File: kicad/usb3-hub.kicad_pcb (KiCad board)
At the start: 6 copper layers, 70 x 140 mm, 218 parts, among them J1001 USB3_A, J101 DISPLAY, J102 USB3_B_Micro, J103 Barrel_Jack_Switch, J201 Conn_01x05_Pin, J301 Debug, J302 Conn_01x03_Pin, J501 USB3_A, J601 USB3_A, J701 USB3_A, J801 USB3_A, J901 USB3_A, Q303 2N7002, SW1001 SW_Push, SW301 SW_Push, SW501 SW_Push, SW601 SW_Push, SW701 SW_Push, SW801 SW_Push, SW901 SW_Push, U1001 AP22804AW5, U201 USB5807, U301 W25Q16JVSS, U302 RP2040, U303 AP22804AW5, U401 TLV1117-33, U402 AP7363C-12E, U501 INA381A1, U502 AP22804AW5, U601 INA381A1, U602 AP22804AW5, U701 INA381A1, U702 AP22804AW5, U801 AP22804AW5, U901 AP22804AW5, Y201 25Mhz, Y301 12Mhz

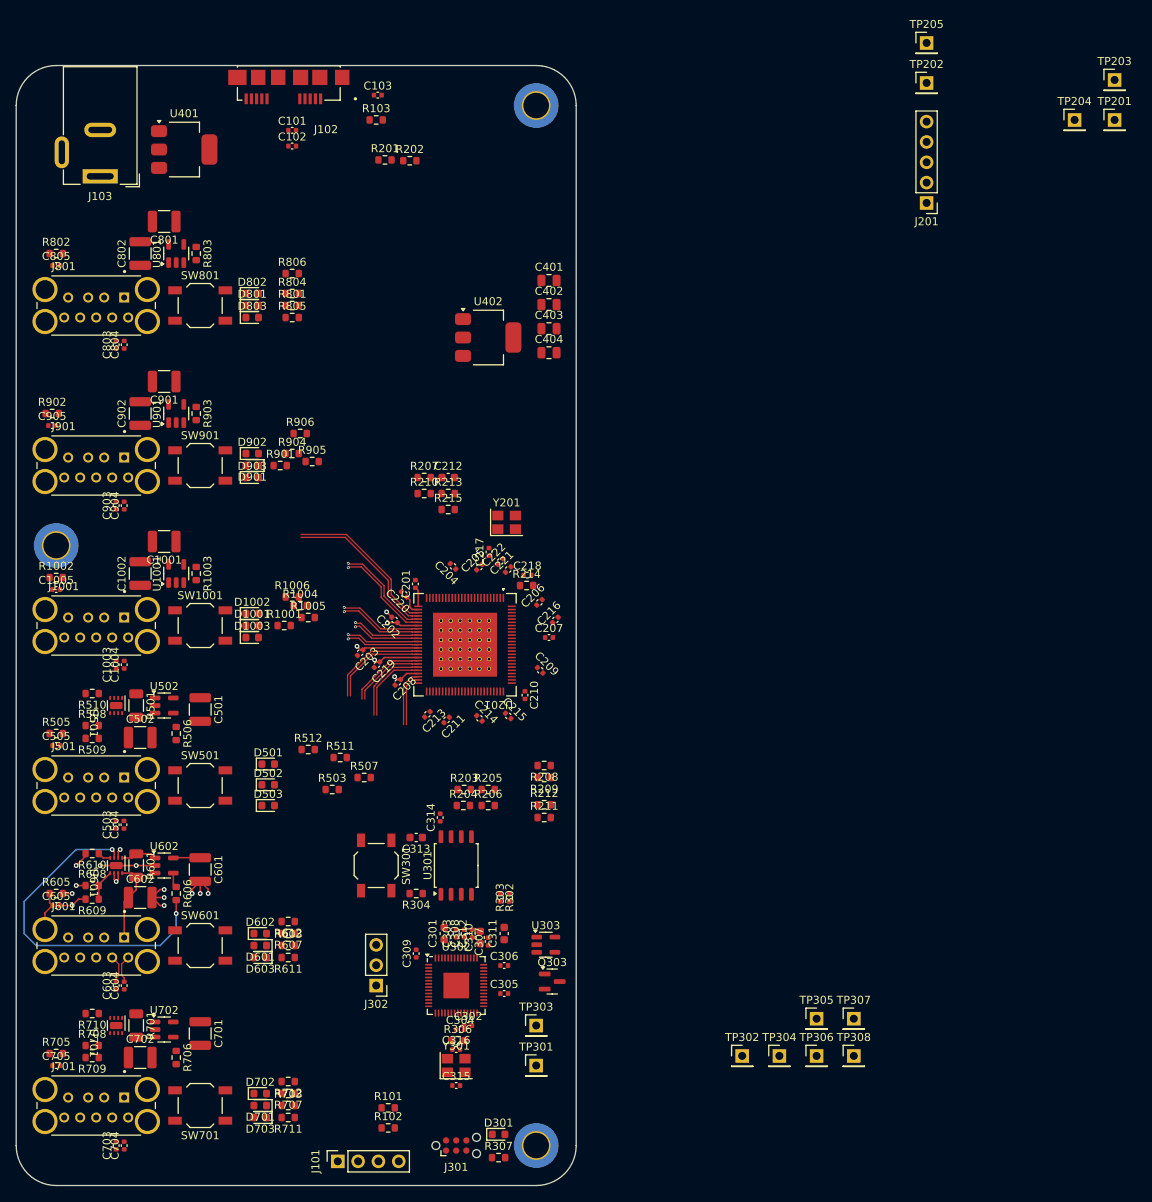
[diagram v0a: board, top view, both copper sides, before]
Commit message: Added first fanout for usb5807
Needs a lot more work, but it is a start, that allows me to concentrate
on the routing of USB signals and have the capacitors relatively close
to the hub controller.
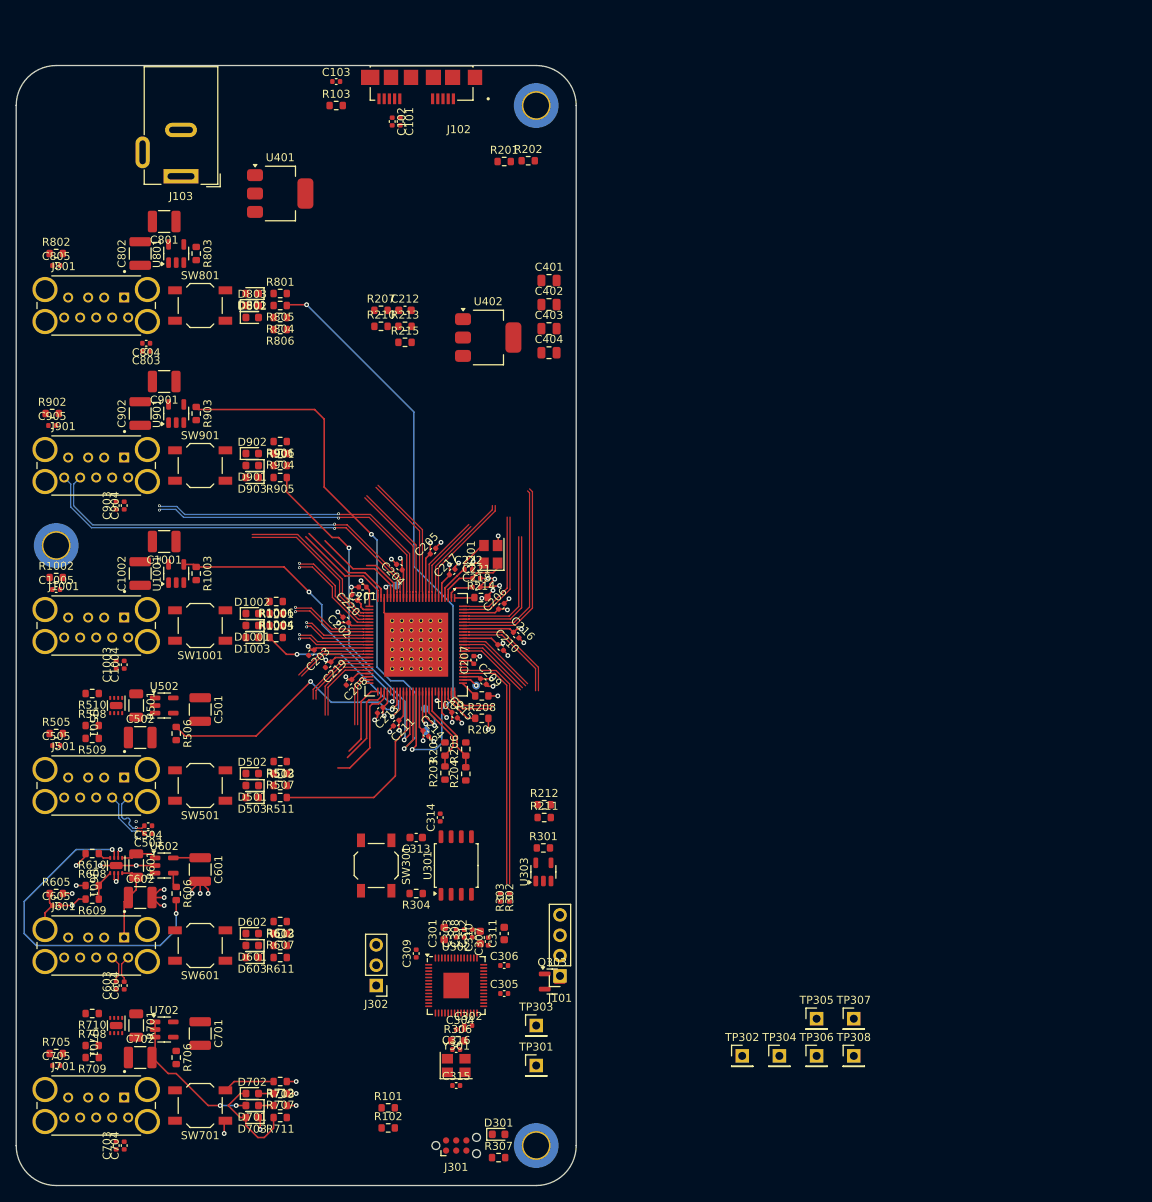
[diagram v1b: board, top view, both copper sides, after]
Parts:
- removed J201: Conn_01x05_Pin, Connector_PinHeader_2.54mm:PinHeader_1x05_P2.54mm_Vertical
- removed TP203: TestPoint, Connector_PinHeader_2.54mm:PinHeader_1x01_P2.54mm_Vertical
- added R301: 100k, Resistor_SMD:R_0603_1608Metric, F.Cu at (165.9, 132.8)
- TP201, TP202, TP204, TP205: footprint Connector_PinHeader_2.54mm:PinHeader_1x01_P2.54mm_Vertical -> TestPoint:TestPoint_Pad_D1.0mm; moved to B.Cu
- moved TP201 115.1 mm to (151.2, 118.2), turned to 180 degrees
- moved TP204 102.9 mm to (147.5, 100.0), turned to 180 degrees
- moved TP202 100.3 mm to (151.1, 115.4), turned to 180 degrees
- moved TP205 98.1 mm to (157.5, 112.5), turned to 180 degrees
- moved J101 36.2 mm to (168.0, 148.8), turned to 180 degrees
- moved C212 21.6 mm to (148.6, 65.6)
- moved R207 21.6 mm to (145.6, 65.6)
- moved R210 21.6 mm to (145.6, 67.6)
- moved R213 21.6 mm to (148.6, 67.6)
- moved R215 21.6 mm to (148.6, 69.6)
- moved J102 16.6 mm to (150.0, 39.2)
- moved R201 14.9 mm to (161.0, 47.0)
- moved R202 14.8 mm to (164.0, 46.9)
- moved C101 13.5 mm to (148.0, 42.0), turned to -90 degrees
- moved U401 13.2 mm to (133.0, 51.0)
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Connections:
- net /Port1/VBUS_HIGH renamed /Port4/VBUS_HIGH
- net /Port1/~{Alert} renamed /Port4/~{Alert}
- net /Port2/VBUS_HIGH renamed /Port5/VBUS_HIGH
- net /Port2/~{Alert} renamed /Port5/~{Alert}
- net /Port3/VBUS_HIGH renamed /Port6/VBUS_HIGH
- net /Port3/~{Alert} renamed /Port6/~{Alert}
- net /Port4/~{Flag} renamed /Port1/~{Flag}
- net /Port5/~{Flag} renamed /Port2/~{Flag}
- net /Port6/~{Flag} renamed /Port3/~{Flag}
- C1002 pad 1: /Port6/VBUS -> /Port3/VBUS
- C1003 pad 2: /Port6/B_SSTX- -> /Port3/B_SSTX-
- C1004 pad 2: /Port6/B_SSTX+ -> /Port3/B_SSTX+
- C1005 pad 1: /Port6/Shield -> /Port3/Shield
- C502 pad 1: /Port1/VBUS -> /Port4/VBUS
- C503 pad 2: /Port1/B_SSTX- -> /Port4/B_SSTX-
- C504 pad 2: /Port1/B_SSTX+ -> /Port4/B_SSTX+
- C505 pad 1: /Port1/Shield -> /Port4/Shield
- C602 pad 1: /Port2/VBUS -> /Port5/VBUS
- C603 pad 2: /Port2/B_SSTX- -> /Port5/B_SSTX-
- C604 pad 2: /Port2/B_SSTX+ -> /Port5/B_SSTX+
- C605 pad 1: /Port2/Shield -> /Port5/Shield
- C702 pad 1: /Port3/VBUS -> /Port6/VBUS
- C703 pad 2: /Port3/B_SSTX- -> /Port6/B_SSTX-
- C704 pad 2: /Port3/B_SSTX+ -> /Port6/B_SSTX+
- C705 pad 1: /Port3/Shield -> /Port6/Shield
- C802 pad 1: /Port4/VBUS -> /Port1/VBUS
- C803 pad 2: /Port4/B_SSTX- -> /Port1/B_SSTX-
- C804 pad 2: /Port4/B_SSTX+ -> /Port1/B_SSTX+
- C805 pad 1: /Port4/Shield -> /Port1/Shield
- C902 pad 1: /Port5/VBUS -> /Port2/VBUS
- C903 pad 2: /Port5/B_SSTX- -> /Port2/B_SSTX-
- C904 pad 2: /Port5/B_SSTX+ -> /Port2/B_SSTX+
- C905 pad 1: /Port5/Shield -> /Port2/Shield
- D1001 pad 2: /Port6/VBUS -> /Port3/VBUS
- D801 pad 2: /Port4/VBUS -> /Port1/VBUS
- D901 pad 2: /Port5/VBUS -> /Port2/VBUS
- J1001 pad 1: /Port6/VBUS -> /Port3/VBUS
- J1001 pad 10: /Port6/Shield -> /Port3/Shield
- J1001 pad 8: /Port6/B_SSTX- -> /Port3/B_SSTX-
- J1001 pad 9: /Port6/B_SSTX+ -> /Port3/B_SSTX+
- J501 pad 1: /Port1/VBUS -> /Port4/VBUS
- J501 pad 10: /Port1/Shield -> /Port4/Shield
- J501 pad 8: /Port1/B_SSTX- -> /Port4/B_SSTX-
- J501 pad 9: /Port1/B_SSTX+ -> /Port4/B_SSTX+
- J601 pad 1: /Port2/VBUS -> /Port5/VBUS
- J601 pad 10: /Port2/Shield -> /Port5/Shield
- J601 pad 8: /Port2/B_SSTX- -> /Port5/B_SSTX-
- J601 pad 9: /Port2/B_SSTX+ -> /Port5/B_SSTX+
- J701 pad 1: /Port3/VBUS -> /Port6/VBUS
- J701 pad 10: /Port3/Shield -> /Port6/Shield
- J701 pad 8: /Port3/B_SSTX- -> /Port6/B_SSTX-
- J701 pad 9: /Port3/B_SSTX+ -> /Port6/B_SSTX+
- J801 pad 1: /Port4/VBUS -> /Port1/VBUS
- J801 pad 10: /Port4/Shield -> /Port1/Shield
- J801 pad 8: /Port4/B_SSTX- -> /Port1/B_SSTX-
- J801 pad 9: /Port4/B_SSTX+ -> /Port1/B_SSTX+
- J901 pad 1: /Port5/VBUS -> /Port2/VBUS
- J901 pad 10: /Port5/Shield -> /Port2/Shield
- J901 pad 8: /Port5/B_SSTX- -> /Port2/B_SSTX-
- J901 pad 9: /Port5/B_SSTX+ -> /Port2/B_SSTX+
- R1002 pad 1: /Port6/Shield -> /Port3/Shield
- R501 pad 2: /Port1/VBUS -> /Port4/VBUS
- R505 pad 1: /Port1/Shield -> /Port4/Shield
- R601 pad 2: /Port2/VBUS -> /Port5/VBUS
- R605 pad 1: /Port2/Shield -> /Port5/Shield
- R701 pad 2: /Port3/VBUS -> /Port6/VBUS
- R705 pad 1: /Port3/Shield -> /Port6/Shield
- R802 pad 1: /Port4/Shield -> /Port1/Shield
- R902 pad 1: /Port5/Shield -> /Port2/Shield
- TP201 pad 1: /Hub/~{RESET} -> Net-(U201A-SPI_CLK)
- TP202 pad 1: Net-(U201A-GPIO69) -> Net-(U201A-SPI_DO)
- U1001 pad 1: /Port6/VBUS -> /Port3/VBUS
- U201 pad 65: /Hub/SPI_CLK -> Net-(U201A-SPI_CLK)
- U201 pad 66: /Hub/SPI_DO -> Net-(U201A-SPI_DO)
- U201 pad 69: Net-(U201A-GPIO69) -> unconnected-(U201A-GPIO69-Pad69)
- U501 pad 8: /Port1/VBUS -> /Port4/VBUS
- U601 pad 8: /Port2/VBUS -> /Port5/VBUS
- U701 pad 8: /Port3/VBUS -> /Port6/VBUS
- U801 pad 1: /Port4/VBUS -> /Port1/VBUS
- U901 pad 1: /Port5/VBUS -> /Port2/VBUS
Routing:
- net /Hub/Port1.SPEED_IND: track 0.00 -> 77.0 mm, vias 0 -> 2
- net /Hub/Port2.PRT_CTRL: track 0.00 -> 71.7 mm, vias 0 -> 2
- net /Hub/Port2.SSRX-: track 0.00 -> 51.0 mm, vias 0 -> 1
- net /Hub/Port2.SSRX+: track 0.00 -> 51.0 mm, vias 0 -> 1
- net /Hub/Port2.SPEED_IND: track 0.00 -> 45.9 mm, vias 0 -> 2
- net /Hub/Port3.PRT_CTRL: track 0.00 -> 41.2 mm, vias 0 -> 2
- net /Hub/Port2.SSTX+: track 0.00 -> 39.4 mm, vias 0 -> 2
- net /Hub/Port2.SSTX-: track 0.00 -> 38.8 mm, vias 0 -> 2
- net GND: track 25.3 -> 62.9 mm, vias 12 -> 37
- net +3V3: track 10.7 -> 45.8 mm, vias 3 -> 13
- net +1V2: track 17.9 -> 52.8 mm, vias 3 -> 10
- net /Hub/Port4.PRT_CTRL: track 0.00 -> 34.2 mm, vias 0 -> 2
- net /Hub/Port7.DP-: track 0.00 -> 31.5 mm
- net /Hub/Port7.DP+: track 0.00 -> 30.9 mm
- net /Hub/Port4.SPEED_IND: track 0.00 -> 25.8 mm
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
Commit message: Some more routing
Not done, but done some more. Nothing is final, just to get a
better feeling of what could be done.
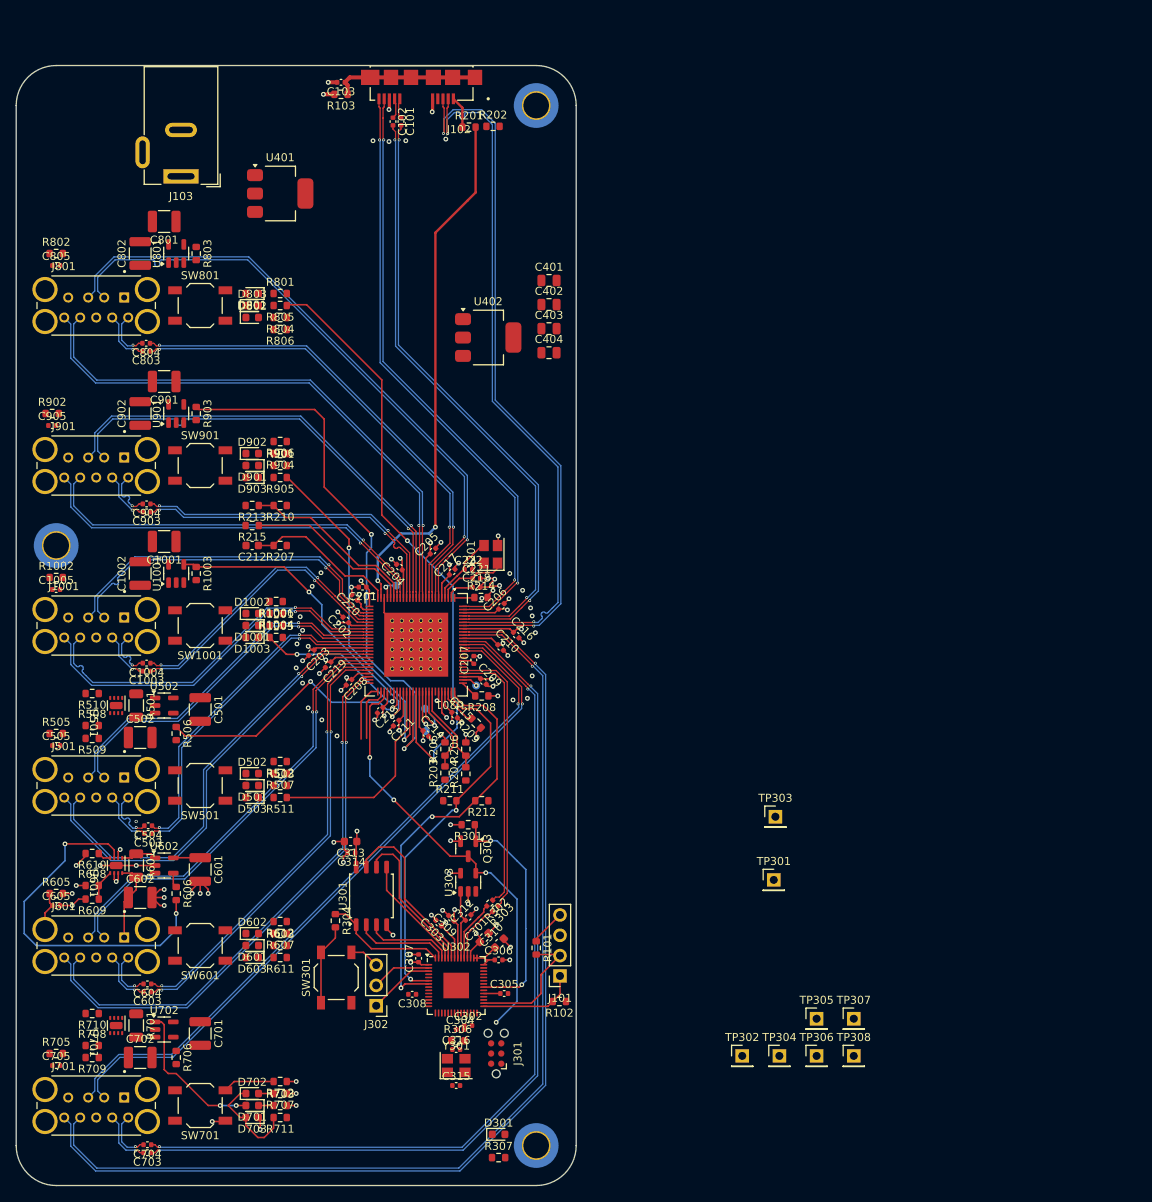
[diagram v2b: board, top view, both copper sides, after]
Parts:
- removed C311: 2.2uF, Capacitor_SMD:C_0603_1608Metric
- moved TP303 39.7 mm to (194.9, 128.9)
- moved TP301 37.7 mm to (194.7, 136.8)
- moved C212 35.1 mm to (129.5, 95.0), turned to 180 degrees
- moved R207 32.0 mm to (133.0, 95.0), turned to 180 degrees
- moved R215 29.8 mm to (129.5, 92.5), turned to 180 degrees
- moved R213 29.4 mm to (129.5, 90.0), turned to 180 degrees
- moved R101 27.2 mm to (165.0, 145.3), turned to -90 degrees
- moved R102 26.6 mm to (167.9, 152.0), turned to 180 degrees
- moved R210 25.7 mm to (133.0, 90.0), turned to 180 degrees
- moved Q303 19.6 mm to (156.5, 132.9), turned to -90 degrees
- moved SW301 14.9 mm to (140.0, 149.0), turned to 90 degrees
- moved J301 12.5 mm to (160.0, 158.5), turned to 90 degrees
- moved R211 12.0 mm to (154.2, 126.9)
- moved C314 11.9 mm to (141.9, 133.4), turned to 180 degrees
- moved U301 11.3 mm to (144.4, 138.8)
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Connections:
- C101 pad 2: /Hub/Port0.SSTX- -> /Hub/Port0.SSTX+
- C102 pad 2: /Hub/Port0.SSTX+ -> /Hub/Port0.SSTX-
- J102 pad 10: /Hub/Port0.SSRX+ -> /Hub/Port0.SSRX-
- J102 pad 9: /Hub/Port0.SSRX- -> /Hub/Port0.SSRX+
- TP304 pad 1: Net-(U302-GPIO18) -> Net-(U302-GPIO7)
- U302 pad 29: Net-(U302-GPIO18) -> /Raspberry/I2C1_SDA
- U302 pad 30: /Hub/Port7.PRT_CTRL -> /Raspberry/I2C1_SCL
- U302 pad 31: /Hub/~{RESET} -> /Hub/Port7.PRT_CTRL
- U302 pad 35: Net-(Q303-G) -> unconnected-(U302-GPIO23-Pad35)
- U302 pad 36: unconnected-(U302-GPIO24-Pad36) -> Net-(Q303-G)
- U302 pad 8: /Raspberry/I2C1_SDA -> /Hub/~{RESET}
- U302 pad 9: /Raspberry/I2C1_SCL -> Net-(U302-GPIO7)
- U501 pad 6: /ADC0 -> /ADC2
- U501 pad 7: /ADC0 -> /ADC2
- U701 pad 6: /ADC2 -> /ADC0
- U701 pad 7: /ADC2 -> /ADC0
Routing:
- net /Hub/Port6.SSRX-: track 14.2 -> 133.0 mm, vias 0 -> 1
- net /Hub/Port6.SSRX+: track 13.6 -> 131.2 mm, vias 0 -> 1
- net /Hub/Port6.SSTX-: track 10.3 -> 112.2 mm, vias 0 -> 2
- net /Hub/Port6.SSTX+: track 9.96 -> 111.0 mm, vias 0 -> 2
- net /Hub/Port6.DP-: track 9.49 -> 86.9 mm, vias 0 -> 1
- net /Hub/Port6.DP+: track 9.19 -> 86.3 mm, vias 0 -> 1
- net /Hub/Port0.DP-: track 23.7 -> 90.7 mm, vias 0 -> 2
- net /Hub/Port0.DP+: track 24.6 -> 90.8 mm, vias 0 -> 2
- net /Hub/Port1.DP+: track 14.5 -> 78.8 mm, vias 0 -> 1
- net /Hub/Port1.DP-: track 14.5 -> 78.8 mm, vias 0 -> 1
- net /Hub/Port5.SSRX-: track 6.63 -> 70.1 mm, vias 0 -> 1
- net /Hub/Port5.SSRX+: track 7.23 -> 69.5 mm, vias 0 -> 1
- net /Hub/Port0.SSRX+: track 16.0 -> 75.9 mm, vias 0 -> 2
- net /Hub/Port0.SSRX-: track 15.4 -> 75.2 mm, vias 0 -> 2
- net /Hub/Port0.SSTX-: track 16.2 -> 76.0 mm, vias 0 -> 2
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- added copper zone on In3.Cu, net /Raspberry/RPI_1V1

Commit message: Add check for DRC
Only checking errors at the moment, as the board is not ready yet
Moved unconnected Items to severity warning.
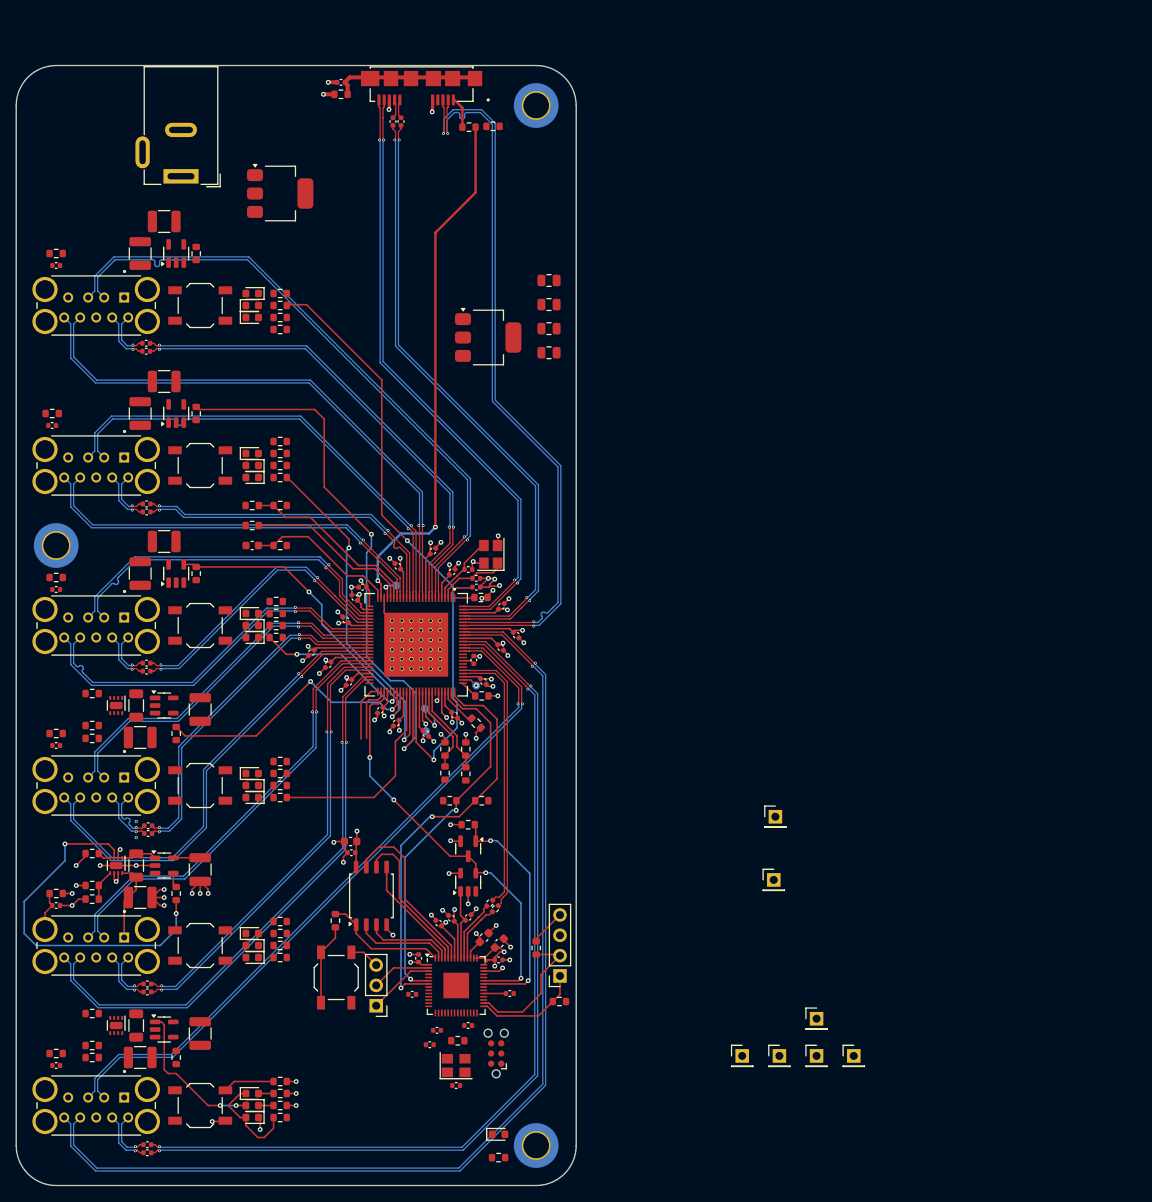
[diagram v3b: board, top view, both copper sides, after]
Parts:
- removed TP307: TestPoint, Connector_PinHeader_2.54mm:PinHeader_1x01_P2.54mm_Vertical
- moved C316 3.35 mm to (151.7, 157.4)
- moved C304 2.90 mm to (152.6, 155.6)
- moved C305 0.70 mm to (161.7, 151.0)
- moved C204 0.22 mm to (147.7, 97.6)
- moved J102 0.14 mm to (150.0, 39.3)
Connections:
- TP306 pad 1: Net-(U302-GPIO25) -> Net-(U302-GPIO20)
- U302 pad 31: /Hub/Port7.PRT_CTRL -> Net-(U302-GPIO20)
- U302 pad 37: Net-(U302-GPIO25) -> /Hub/Port7.PRT_CTRL
- U302 pad 41: /ADC3 -> unconnected-(U302-GPIO29_ADC3-Pad41)
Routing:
- net +3V3: track 72.7 -> 77.4 mm, vias 17 -> 19
- net /ADC2: track 0.00 -> 2.53 mm, vias 0 -> 1
- net /Hub/Port7.PRT_CTRL: track 53.8 -> 52.2 mm
- net /Raspberry/I2C1_SDA: track 12.5 -> 13.5 mm
- net /Raspberry/I2C1_SCL: track 16.4 -> 17.3 mm
- net (no net): vias 23 -> 0
